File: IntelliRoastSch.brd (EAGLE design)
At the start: 53.3 x 76.2 mm, 26 parts, among them U1 LM2576HVS-3.3/NOPB

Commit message: added power and ground connections to F207 Headers, connected BT pins to F207 Headers, Added jumpers to configure power delivery to F207
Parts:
- removed JP1, JP3: (no value), pinhead:1X06
- added EXT_12V, EXT_3V3: (no value), pinhead:1X02
- added TEMP1, TEMP2: (no value), pinhead:1X06
- moved 12V_TERM 71.2 mm to (8.89, 71.9), turned to 180 degrees
- moved FAN_TERM 69.8 mm to (18.8, 71.9), turned to 180 degrees
- moved Q2 50.2 mm to (37.6, 64.5), turned to 180 degrees
- moved D1 27.0 mm to (26.2, 66.3)
- moved BT_HEADER 21.5 mm to (18.0, -6.86)
- moved U1 18.1 mm to (21.1, 39.9), turned to 0 degrees
- moved L1 17.4 mm to (36.6, 38.9)
- moved MIC_HEADER 6.97 mm to (13.2, 55.6), turned to 270 degrees
- renumbered JP2 to TEMP0, JP8 to TEMP3
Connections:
- removed net N$100: CN10.23
- removed net N$101: CN10.25
- removed net N$102: CN10.27
- removed net N$104: CN10.31
- removed net N$105: CN10.33
- removed net N$106: CN10.34
- removed net N$107: CN10.32
- removed net N$108: CN10.30
- removed net N$109: CN10.28
- removed net N$110: CN10.26
- removed net N$111: CN10.24
- removed net N$112: CN10.22
- removed net N$113: CN10.20
- removed net N$114: CN10.18
- removed net N$115: CN10.16
- removed net N$116: CN10.14
- removed net N$117: CN10.12
- removed net N$118: CN10.10
- removed net N$20: CN8.3
- removed net N$25: CN8.5
- removed net N$26: CN8.7
- removed net N$27: CN8.9
- removed net N$28: CN8.11
- removed net N$29: CN8.13
- removed net N$30: CN8.15
- removed net N$31: CN8.16
- removed net N$32: CN8.14
- removed net N$33: CN8.12
- removed net N$34: CN8.10
- removed net N$35: CN8.8
- removed net N$36: CN8.6
- removed net N$37: CN8.4
- removed net N$38: CN8.2
- removed net N$40: CN9.3
- removed net N$41: CN9.5
- removed net N$42: CN9.7
- removed net N$43: CN9.9
- removed net N$44: CN9.11
- removed net N$45: CN8.1, CN9.13
- removed net N$46: CN9.15
- removed net N$47: CN9.17
- removed net N$48: CN9.19
- removed net N$49: CN9.21
- removed net N$50: CN9.23
- removed net N$51: CN9.25
- removed net N$52: CN9.27
- removed net N$53: CN9.29
- removed net N$54: CN9.30
- removed net N$55: CN9.28
- removed net N$56: CN9.26
- removed net N$57: CN9.24
- removed net N$58: CN9.22
- removed net N$59: CN9.20
- removed net N$60: CN9.18
- removed net N$61: CN9.16
- removed net N$62: CN9.14
- removed net N$63: CN9.12
- removed net N$64: CN9.10
- removed net N$65: CN9.8
- removed net N$67: CN9.4
- removed net N$68: CN9.2
- removed net N$70: CN7.3
- removed net N$71: CN7.5
- removed net N$72: CN7.7
- removed net N$73: CN7.9
- removed net N$74: CN7.11
- removed net N$76: CN7.15
- removed net N$77: CN7.17
- removed net N$78: CN7.19
- removed net N$79: CN7.2
- removed net N$80: CN7.4
- removed net N$81: CN7.6
- removed net N$82: CN7.8
- removed net N$85: CN7.14
- removed net N$86: CN7.16
- removed net N$87: CN7.18
- removed net N$88: CN7.20
- removed net N$89: CN10.1
- removed net N$90: CN10.3
- removed net N$91: CN10.5
- removed net N$93: CN10.9
- removed net N$94: CN10.11
- removed net N$95: CN10.13
- removed net N$96: CN10.15
- removed net N$97: CN10.17
- removed net N$98: CN10.19
- removed net SPI1_MOSI: CN7.13
- new net N$2: CN8.7, EXT_3V3.2
- new net N$3: CN8.15, EXT_12V.2
- net +12V: now also EXT_12V.1
- net +3V3: now also EXT_3V3.1, TEMP1.6, TEMP2.6; no longer JP1.6, JP3.6
- net BT_ENABLE: now also CN10.10
- net BT_STATE: now also CN10.12
- net GND: now also CN10.15, CN10.17, CN10.22, CN10.27, CN10.5, CN7.8, CN8.11, CN8.13, CN9.12, CN9.23, TEMP1.4, TEMP2.4; no longer JP1.4, JP3.4
- net SPI1_CS2: now also TEMP2.2; no longer JP1.2
- net SPI1_MISO: now also TEMP1.3, TEMP2.3; no longer JP1.3, JP3.3
- net SPI1_SCK: now also TEMP1.1, TEMP2.1; no longer JP1.1, JP3.1
- net SPI2_CS1: now also TEMP1.2; no longer JP3.2
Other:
- board size 53.3 x 76.2 mm -> 53.3 x 94.5 mm

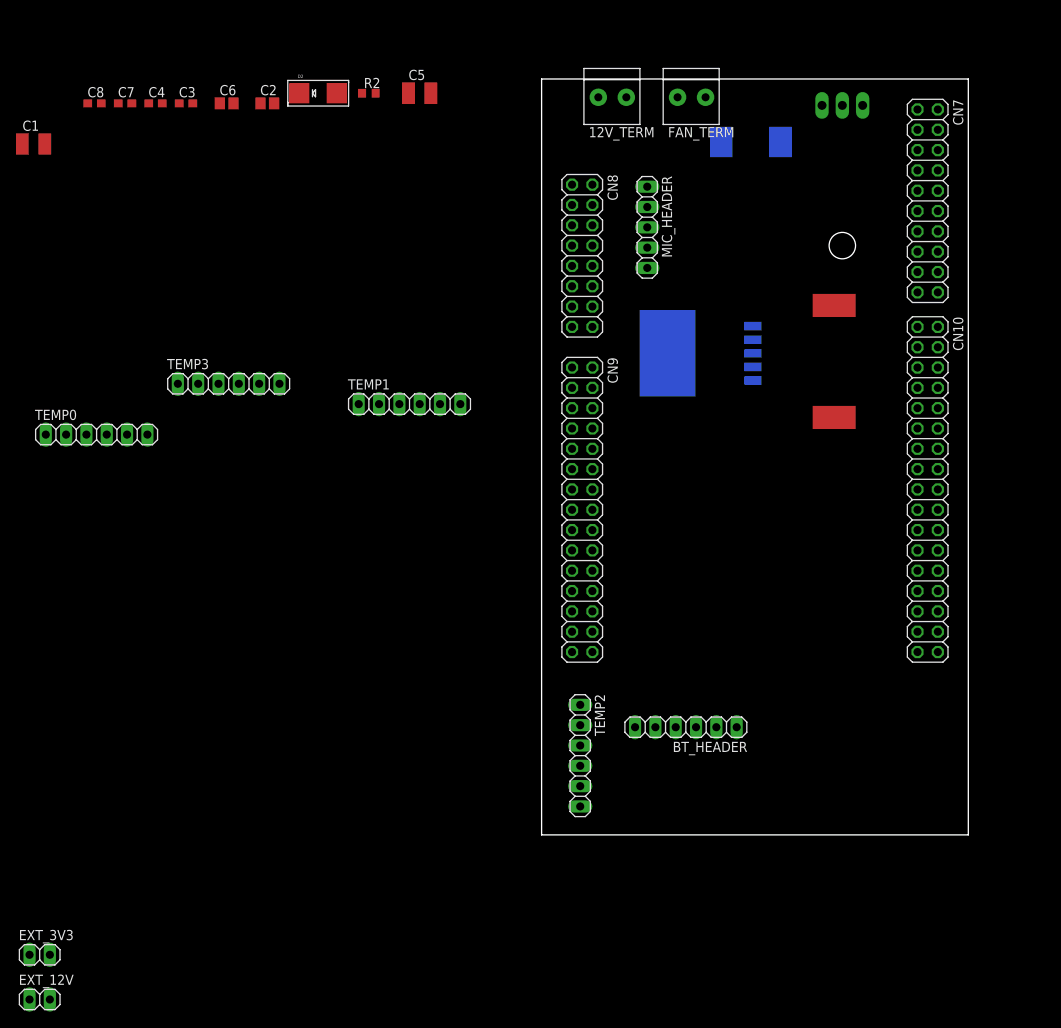
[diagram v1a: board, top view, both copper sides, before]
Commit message: Arranged the components on board, need to add gnd, 3v3, 12v, and gnd planes and then start to route board
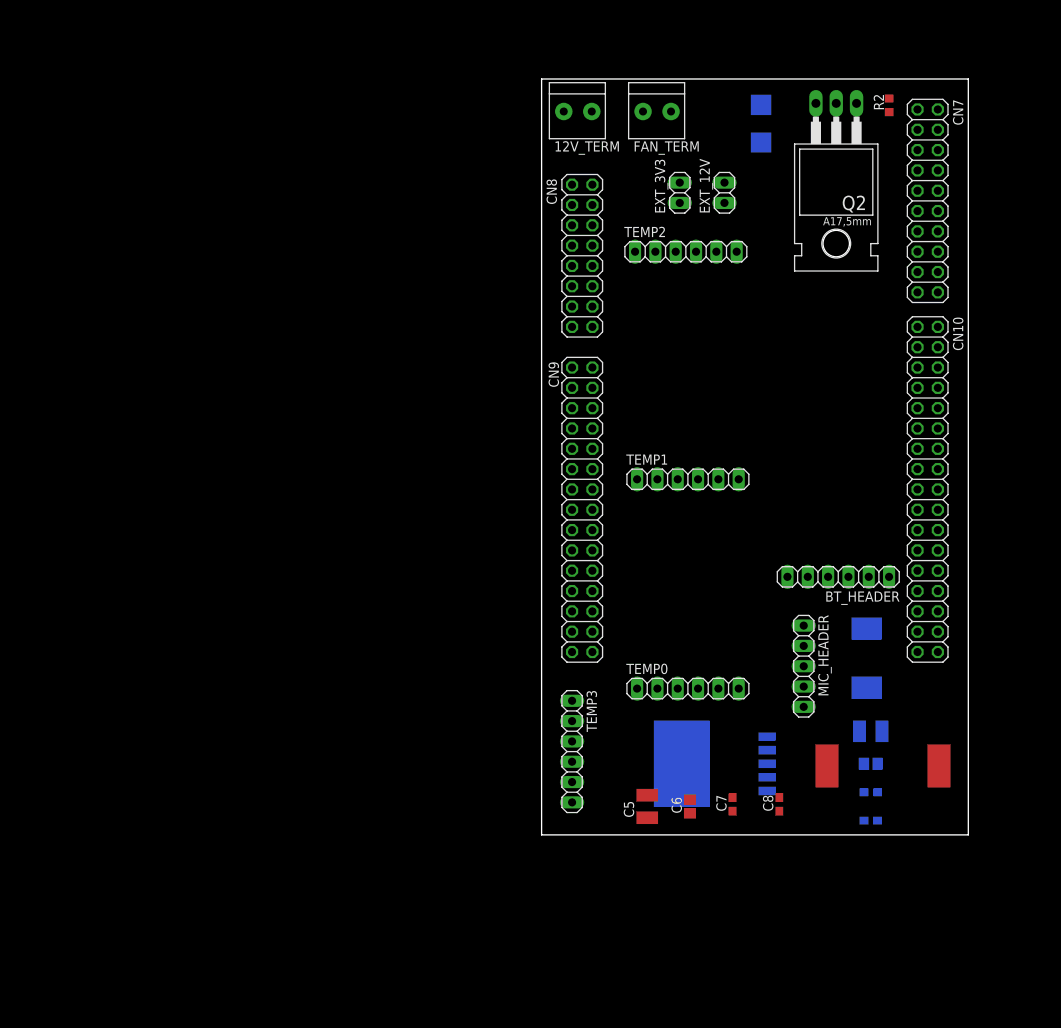
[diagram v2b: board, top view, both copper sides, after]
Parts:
- C1, C5: value (none) -> 100uF
- C2, C6: value (none) -> 10uF
- C3, C4, C7, C8: value (none) -> 0.1uF
- moved EXT_12V 132.3 mm to (22.9, 59.9), turned to 90 degrees
- moved C1 127.8 mm to (41.1, -7.37), flipped to the bottom
- moved C4 126.6 mm to (41.1, -18.5), flipped to the bottom
- moved EXT_3V3 124.4 mm to (17.3, 59.9), turned to 90 degrees
- moved C8 122.5 mm to (29.7, -16.5), turned to 90 degrees
- moved C3 121.4 mm to (41.1, -15.0), flipped to the bottom
- moved C7 116.0 mm to (23.9, -16.5), turned to 90 degrees
- moved C2 111.8 mm to (41.1, -11.4), flipped to the bottom
- moved C6 105.2 mm to (18.5, -16.8), turned to 90 degrees
- moved C5 93.6 mm to (13.2, -16.8), turned to 90 degrees
- moved TEMP0 80.4 mm to (18.3, -2.03)
- moved D1 66.1 mm to (40.6, 1.78), turned to 90 degrees
- moved R2 65.0 mm to (43.4, 70.9), turned to 90 degrees
- moved TEMP2 64.4 mm to (18.0, 52.6), turned to 0 degrees
- moved TEMP3 62.9 mm to (3.81, -9.91), turned to 270 degrees
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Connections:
- net N$1 renamed OUT

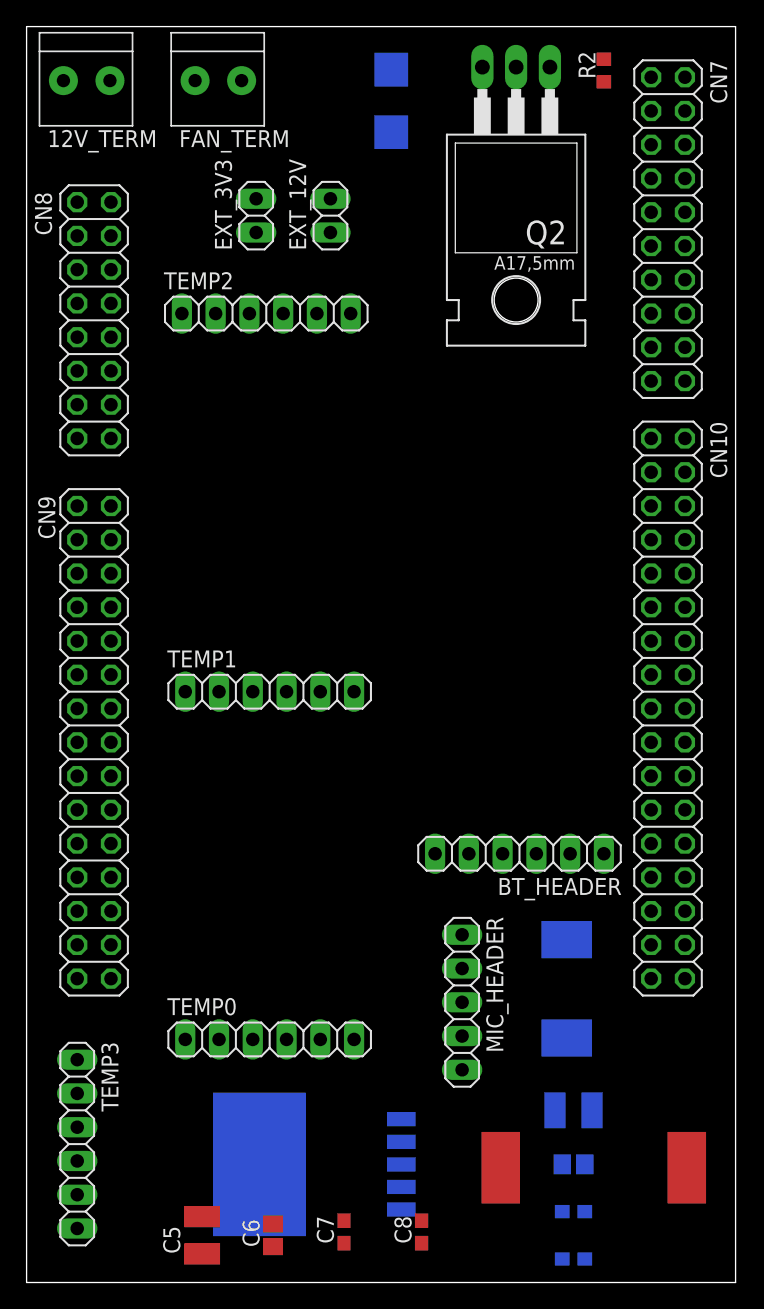
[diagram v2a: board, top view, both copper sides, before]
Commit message: Routed Board and added GND Planes to top and bottom
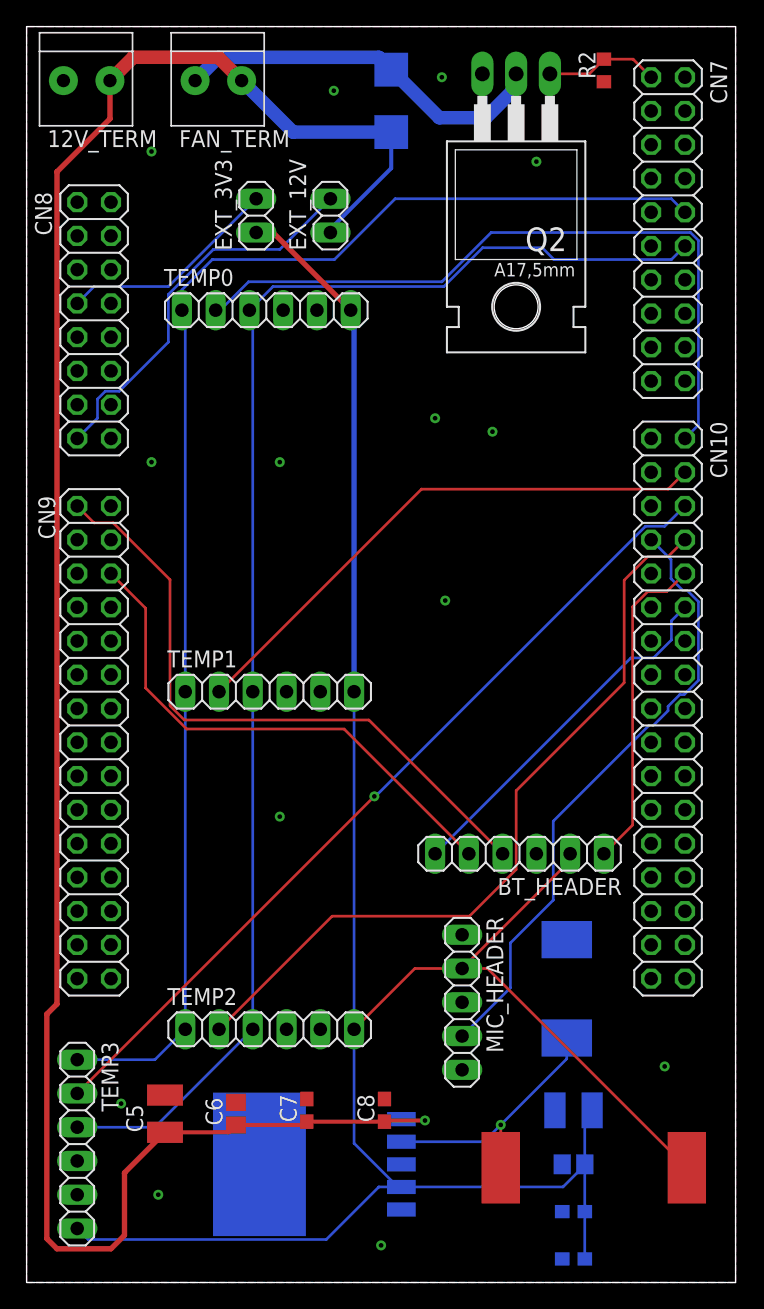
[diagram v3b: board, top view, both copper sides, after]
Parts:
- moved TEMP0 54.9 mm to (18.0, 52.8)
- moved TEMP2 53.8 mm to (18.3, -1.27)
- moved C7 9.56 mm to (21.1, -7.37)
- moved C8 9.56 mm to (26.9, -7.37)
- moved C5 9.56 mm to (10.4, -7.62)
- moved C6 9.56 mm to (15.7, -7.62)
- moved Q2 0.51 mm to (36.8, 64.3)
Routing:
- net +3V3: track 0.00 -> 174.7 mm
- net +12V: track 0.00 -> 160.1 mm, vias 0 -> 1
- net SPI1_MISO: track 0.00 -> 106.0 mm
- net SPI1_SCK: track 0.00 -> 105.9 mm
- net SPI1_CS3: track 0.00 -> 64.0 mm, vias 0 -> 1
- net SPI1_CS2: track 0.00 -> 58.3 mm
- net SPI2_CS0: track 0.00 -> 54.3 mm
- net BT_RX: track 0.00 -> 48.4 mm
- net MIC_IN: track 0.00 -> 46.8 mm
- net SPI2_CS1: track 0.00 -> 41.9 mm
- net BT_TX: track 0.00 -> 39.2 mm
- net N$3: track 0.00 -> 29.5 mm
- net FAN_TO_MOS: track 0.00 -> 28.7 mm
- net BT_STATE: track 0.00 -> 27.3 mm
- net BT_ENABLE: track 0.00 -> 24.4 mm
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- added copper zone on layer 1, net GND
- added copper zone on layer 16, net GND

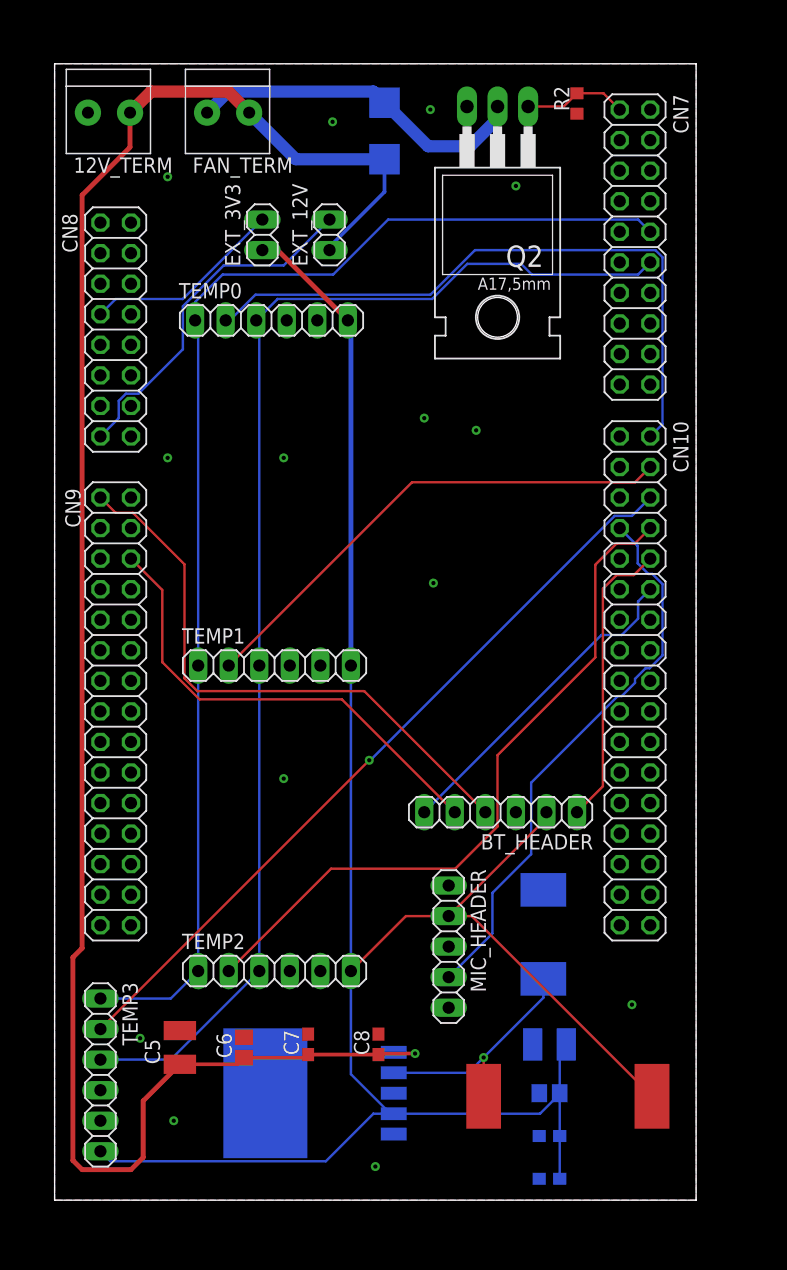
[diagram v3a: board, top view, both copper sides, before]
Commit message: Replaced Mosfet Footprint with virtical instead of horizontal
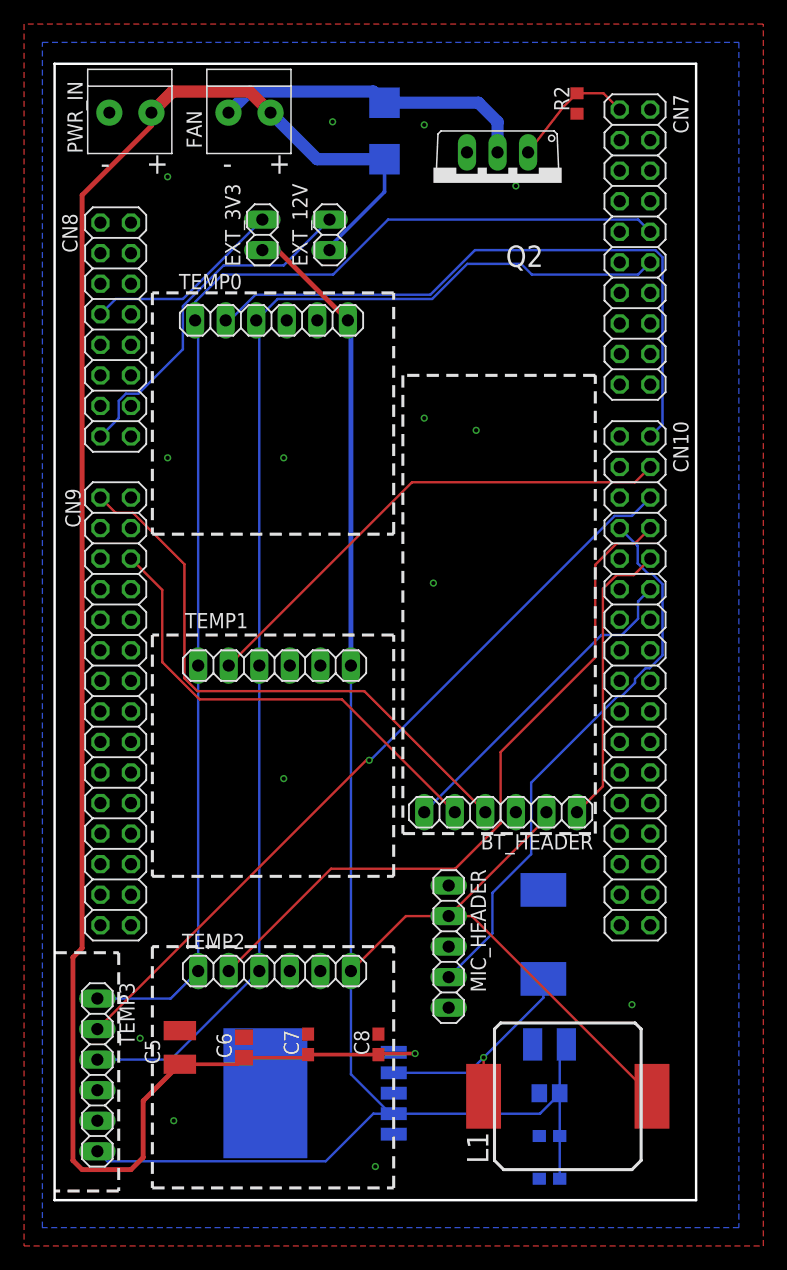
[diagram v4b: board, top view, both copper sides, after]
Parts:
- removed 12V_TERM, FAN_TERM: 1X2-3.5MM, adafruit:1X2-3.5MM
- added FAN, PWR_IN: 1X2-3.5MM, adafruit:1X2-3.5MM
- Q2: device transistor-power:TO220BH -> adafruit:TO220V
- moved TEMP3 0.25 mm to (3.56, -9.91)
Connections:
- net +12V: now also FAN.2, PWR_IN.2; no longer 12V_TERM.2, FAN_TERM.2
- net FAN_TO_MOS: now also FAN.1, Q2.2; no longer FAN_TERM.1, Q2.D
- net GND: now also PWR_IN.1, Q2.3; no longer 12V_TERM.1, Q2.S
- net TIM3_CH1: now also Q2.1; no longer Q2.G
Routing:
- net FAN_TO_MOS: track 28.7 -> 26.7 mm
- net TIM3_CH1: track 8.64 -> 10.5 mm
- net +12V: track 160.1 -> 159.0 mm
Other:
- board text added: "+"
- board text added: "-"
- board text added: "L1"
